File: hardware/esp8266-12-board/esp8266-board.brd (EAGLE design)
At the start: 24.9 x 40 mm, 16 parts, among them P1 ESP8266, P2 ESP8266 CONNECTOR, T1 AMS1117, T2 LM7805

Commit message: generic switch board creation
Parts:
- removed P1: ESP8266, stutz-eagle:PIN-HEADER-4PIN
- removed P2: ESP8266 CONNECTOR, stutz-eagle:PIN-HEADER-4PIN
- removed UART: 3.3V RX TX GND, stutz-eagle:PIN-HEADER-4PIN
- added E1: ESP8266-12, stutz-eagle:ESP8266-12
- added R2, R3: 3k3, stutz-eagle:RESISTOR-V1
- added R4: 10k, stutz-eagle:RESISTOR-V1
- OUTPUT: value GND 3.3V 5V IO0 IO2 -> GND GND 3.3V 5V RX TX; device stutz-eagle:PIN-HEADER-5PIN -> stutz-eagle:PIN-HEADER-6PIN
- R1: value 3k3 -> 470; device stutz-eagle:RESISTOR-V2 -> stutz-eagle:RESISTOR-V1
- moved C1 18.4 mm to (22.1, 35.8), turned to 270 degrees
- moved T1 11.1 mm to (21.8, 7.43), flipped to the top
- moved C2 9.52 mm to (25.2, 14.9)
- moved R1 8.70 mm to (24.3, 27.2)
- moved C7 8.35 mm to (24.7, 21.4), turned to 0 degrees
- moved C5 7.66 mm to (12.0, 7.01)
- moved C4 5.83 mm to (15.3, 7.00), turned to 270 degrees
- moved FIRMWARE 3.72 mm to (25.3, 31.8)
- moved OUTPUT 1.20 mm to (11.4, 37.6)
- moved POWER 1.20 mm to (13.8, 2.54)
- moved C3 0.57 mm to (7.31, 4.08)
- moved T2 0.24 mm to (13.5, 15.0), flipped to the bottom, turned to 270 degrees
- moved C6 0.22 mm to (3.01, 6.99)
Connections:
- new net ESP_GPIO15: E1.2, R2.1
- new net GPIO5: E1.6
- net +3.3V: now also E1.11, E1.16, E1.9, OUTPUT.3, R3.2, R4.1; no longer OUTPUT.2, P1.2, P1.3, P1.4, UART.1
- net +5V: now also OUTPUT.4; no longer OUTPUT.3
- net ESP_GPIO0: now also E1.4, R4.2; no longer OUTPUT.4, P2.3
- net ESP_GPIO2: now also E1.3, R3.1; no longer OUTPUT.5, P2.2
- net ESP_RX: now also E1.7, OUTPUT.5; no longer P2.4, UART.2
- net ESP_TX: now also E1.8, OUTPUT.6; no longer P1.1, UART.3
- net GND: now also E1.1, OUTPUT.2, R2.2; no longer P2.1, UART.4
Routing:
- net +5V: track 64.9 -> 85.5 mm, vias 0 -> 2
- net ESP_GPIO15: track 0.00 -> 15.0 mm
- net +24V: track 28.0 -> 42.4 mm, vias 1 -> 2
- net +3.3V: track 73.6 -> 87.5 mm
- net GND: track 108.1 -> 121.7 mm, vias 3 -> 4
- net ESP_GPIO2: track 21.3 -> 11.0 mm, vias 2 -> 0
- net ESP_GPIO0: track 22.9 -> 15.6 mm, vias 1 -> 0
- net ESP_TX: track 18.4 -> 11.3 mm
- net N$1: track 3.80 -> 7.30 mm
- net ESP_RX: track 14.6 -> 13.7 mm, vias 2 -> 0
- added copper zone on layer 1, net GND
- removed copper zone on layer 1, net N$6
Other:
- board size 24.9 x 40 mm -> 27.9 x 40 mm

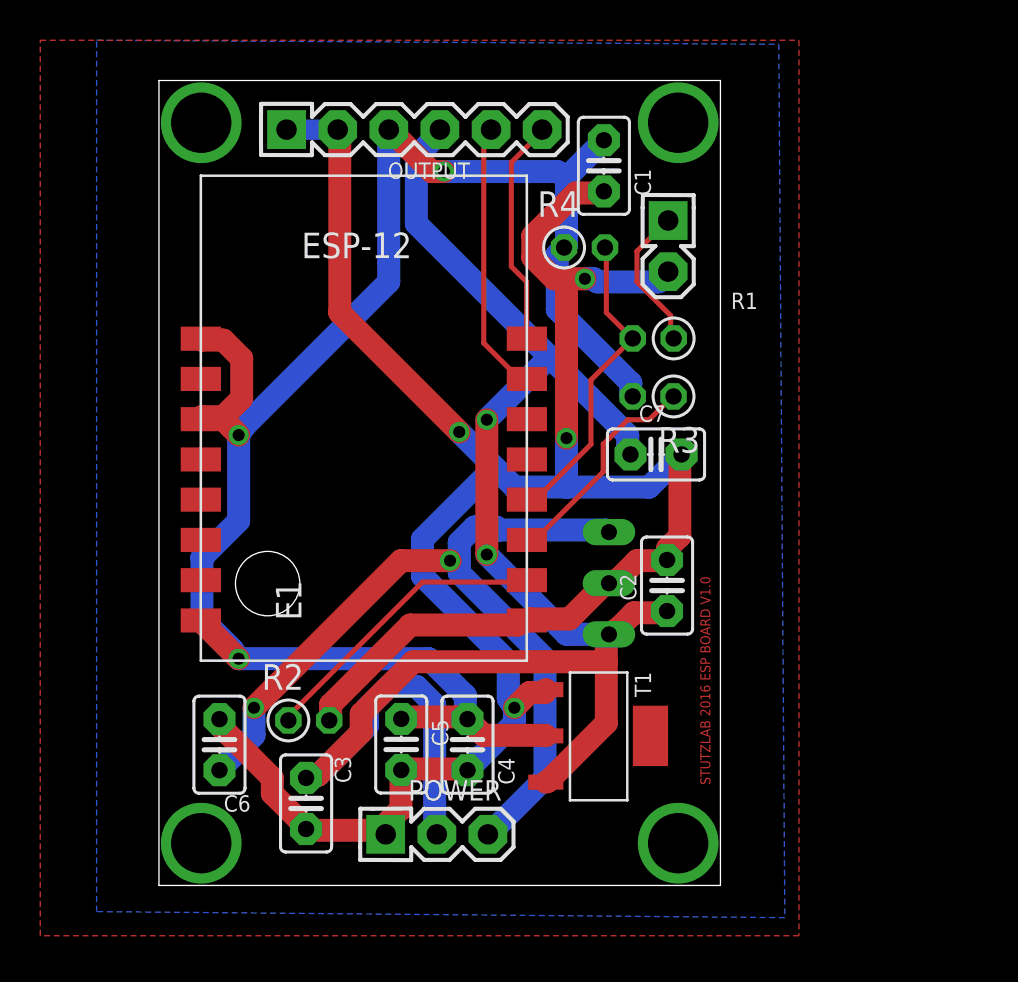
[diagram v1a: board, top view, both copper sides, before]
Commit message: Watchdog and SD card addition to ESP12E
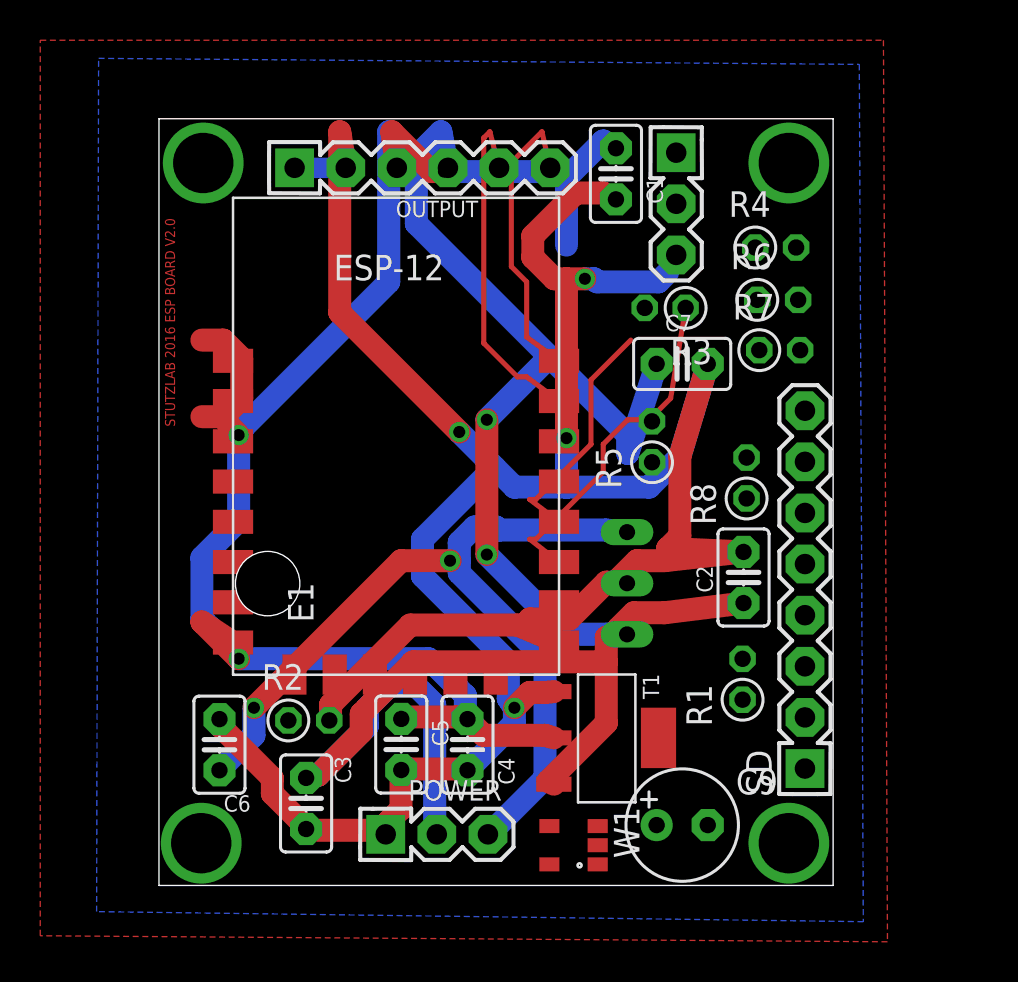
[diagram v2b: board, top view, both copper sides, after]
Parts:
- added C9: 470uF, rcl:E2,5-6
- added R5, R6, R7, R8: 10k, stutz-eagle:RESISTOR-V1
- added SD: PIN-HEADER-8PIN, stutz-eagle:PIN-HEADER-8PIN
- added W1: TPS3823, stutz-eagle:SOT23-5/TSOT25
- FIRMWARE: device stutz-eagle:PIN-HEADER-2PIN -> stutz-eagle:PIN-HEADER-3PIN
- R1: value 470 -> 10k
- R2, R3: value 3k3 -> 10k
- moved R1 17.3 mm to (29.0, 10.5), turned to 90 degrees
- moved R4 9.50 mm to (30.9, 31.7)
- moved C7 4.68 mm to (26.0, 25.9)
- moved R3 4.44 mm to (24.9, 28.7)
- moved C2 3.82 mm to (29.0, 15.3)
- moved FIRMWARE 2.14 mm to (25.7, 33.9)
- moved OUTPUT 1.94 mm to (11.8, 35.7)
- moved E1 1.94 mm to (11.3, 21.5)
- moved T2 0.90 mm to (14.4, 15.0)
- moved C1 0.72 mm to (22.7, 35.4)
- moved T1 0.41 mm to (22.2, 7.33)
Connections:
- removed net N$1: FIRMWARE.1, R1.1
- new net ESP_CH_PD: E1.11, R4.2, W1.1
- new net ESP_RST: E1.9, FIRMWARE.3, R1.2
- new net SD_MISO: E1.21, R7.1, SD.8
- new net SD_MOSI: E1.18, R6.1, SD.3
- new net SD_NC: SD.1
- new net SD_SCK: E1.17, R8.1, SD.6
- net +3.3V: now also C9.+, R1.1, R5.2, R6.2, R7.2, R8.2, SD.5, W1.3, W1.5; no longer E1.11, E1.9
- net ESP_GPIO0: now also FIRMWARE.2, R5.1, W1.4; no longer R1.2, R4.2
- net ESP_GPIO2: now also SD.2
- net GND: now also C9.-, FIRMWARE.1, SD.4, SD.7, W1.2; no longer FIRMWARE.2
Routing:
- net GND: track 121.7 -> 144.8 mm
- net ESP_GPIO15: track 15.0 -> 0.00 mm
- net +5V: track 85.5 -> 97.4 mm
- net N$1: track 7.30 -> 0.00 mm
- net ESP_GPIO2: track 11.0 -> 17.1 mm
- net ESP_TX: track 11.3 -> 15.0 mm
- net ESP_RX: track 13.7 -> 17.3 mm
- net ESP_GPIO0: track 15.6 -> 12.0 mm
- net +3.3V: track 87.5 -> 84.2 mm
- net +24V: track 42.4 -> 43.2 mm
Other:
- board size 27.9 x 40 mm -> 33.5 x 38.1 mm
- board text added: "STUTZLAB 2016 ESP BOARD V2.0"
- board text removed: "ESP8266"
- board text removed: "FEMALE PIN"
- board text removed: "LM7805"
- board text removed: "SOLDERED"
- board text removed: "STUTZLAB 2016 ESP BOARD V1.0"

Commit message: commit
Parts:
- removed SD: PIN-HEADER-8PIN, stutz-eagle:PIN-HEADER-8PIN
- added SD1: CS SI GND 3.3V SCK GND SO, stutz-eagle:PIN-HEADER-7PIN
- FIRMWARE: value FIRMWARE -> GND DTR RTS
- OUTPUT: value GND GND 3.3V 5V RX TX -> GND GND 3.3V 5V RX TX
- moved R4 25.3 mm to (5.60, 30.4), turned to 270 degrees
- moved W1 25.1 mm to (11.0, 25.2), flipped to the bottom, turned to 0 degrees
- moved C7 19.6 mm to (21.7, 6.82)
- moved T1 18.5 mm to (19.3, 25.6), flipped to the bottom, turned to 0 degrees
- moved C4 9.49 mm to (23.8, 2.73), turned to 0 degrees
- moved R8 7.69 mm to (32.8, 27.3)
- moved C1 6.09 mm to (26.3, 30.4), turned to 90 degrees
- moved T2 5.90 mm to (20.3, 15.0)
- moved R7 5.09 mm to (32.8, 21.8), turned to 90 degrees
- moved R3 4.90 mm to (29.6, 27.3), turned to 90 degrees
- moved R5 4.82 mm to (29.3, 21.9)
- moved C9 4.32 mm to (29.2, 5.90), turned to 270 degrees
- moved C2 4.01 mm to (33.0, 15.0)
- moved E1 4.00 mm to (15.3, 21.3)
- moved C5 3.19 mm to (15.2, 6.66), turned to 180 degrees
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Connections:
- removed net SD_NC: SD.1
- net +3.3V: now also SD1.4; no longer SD.5
- net ESP_GPIO2: now also SD1.1; no longer SD.2
- net GND: now also SD1.3, SD1.6; no longer SD.4, SD.7
- net SD_MISO: now also SD1.7; no longer SD.8
- net SD_MOSI: now also SD1.2; no longer SD.3
- net SD_SCK: now also SD1.5; no longer SD.6
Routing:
- net ESP_RST: track 0.00 -> 85.3 mm, vias 0 -> 1
- net SD_MOSI: track 0.00 -> 52.1 mm, vias 0 -> 2
- net SD_SCK: track 0.00 -> 44.2 mm, vias 0 -> 2
- net +3.3V: track 84.2 -> 128.2 mm
- net SD_MISO: track 0.00 -> 39.0 mm, vias 0 -> 1
- net ESP_GPIO2: track 17.1 -> 53.7 mm
- net ESP_GPIO0: track 12.0 -> 40.2 mm, vias 0 -> 1
- net ESP_CH_PD: track 0.00 -> 26.2 mm
- net +5V: track 97.4 -> 73.1 mm, vias 2 -> 3
- net ESP_GPIO15: track 0.00 -> 19.2 mm
- net GND: track 144.8 -> 160.0 mm, vias 4 -> 8
- net +24V: track 43.2 -> 37.4 mm
- net ESP_TX: track 15.0 -> 11.7 mm
- net ESP_RX: track 17.3 -> 15.0 mm
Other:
- board size 33.5 x 38.1 mm -> 35.4 x 38 mm

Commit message: upload part name
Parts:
- W1: value TPS3823 -> TPS3823-33
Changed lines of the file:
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@@
 <attribute name="VALUE" x="34.6892" y="26.9092" size="0.8128" layer="27" ratio="10" rot="R90"/>
 </element>
-<element name="W1" library="stutz-eagle" package="SOT23-5/TSOT25" value="TPS3823" x="11" y="25.2" rot="MR0"/>
+<element name="W1" library="stutz-eagle" package="SOT23-5/TSOT25" value="TPS3823-33" x="11" y="25.2" rot="MR0"/>
 <element name="SD1" library="stutz-eagle" package="PIN-HEADER-7PIN" value="CS  SI GND 3.3V SCK GND SO" x="1.7" y="18.9" smashed="yes" rot="R270">
 <attribute name="VALUE" x="4.333" y="27.99" size="0.9" layer="27" ratio="10" rot="R270"/>

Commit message: updated PCB design during first board assembly
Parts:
- C3, C4: device capacitor-wima:C2.5-2 -> rcl:E2,5-6E
- R1, R2, R3, R4, R5, R6, R7, R8: device stutz-eagle:RESISTOR-V1 -> stutz-components-library:RESISTOR-V1
- T2: device stutz-eagle:TO-220 -> stutz-components-library:TO-220
- moved C7 0.20 mm to (21.7, 7.02)
- moved C3 0.14 mm to (8.18, 2.89)
- moved C4 0.10 mm to (23.8, 2.83)
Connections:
- net +3.3V: now also C4.+; no longer C4.1
- net +5V: now also C3.+; no longer C3.1
- net GND: now also C3.-, C4.-; no longer C3.2, C4.2
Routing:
- net GND: track 160.0 -> 160.9 mm
